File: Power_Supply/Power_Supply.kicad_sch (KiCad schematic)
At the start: 47 parts

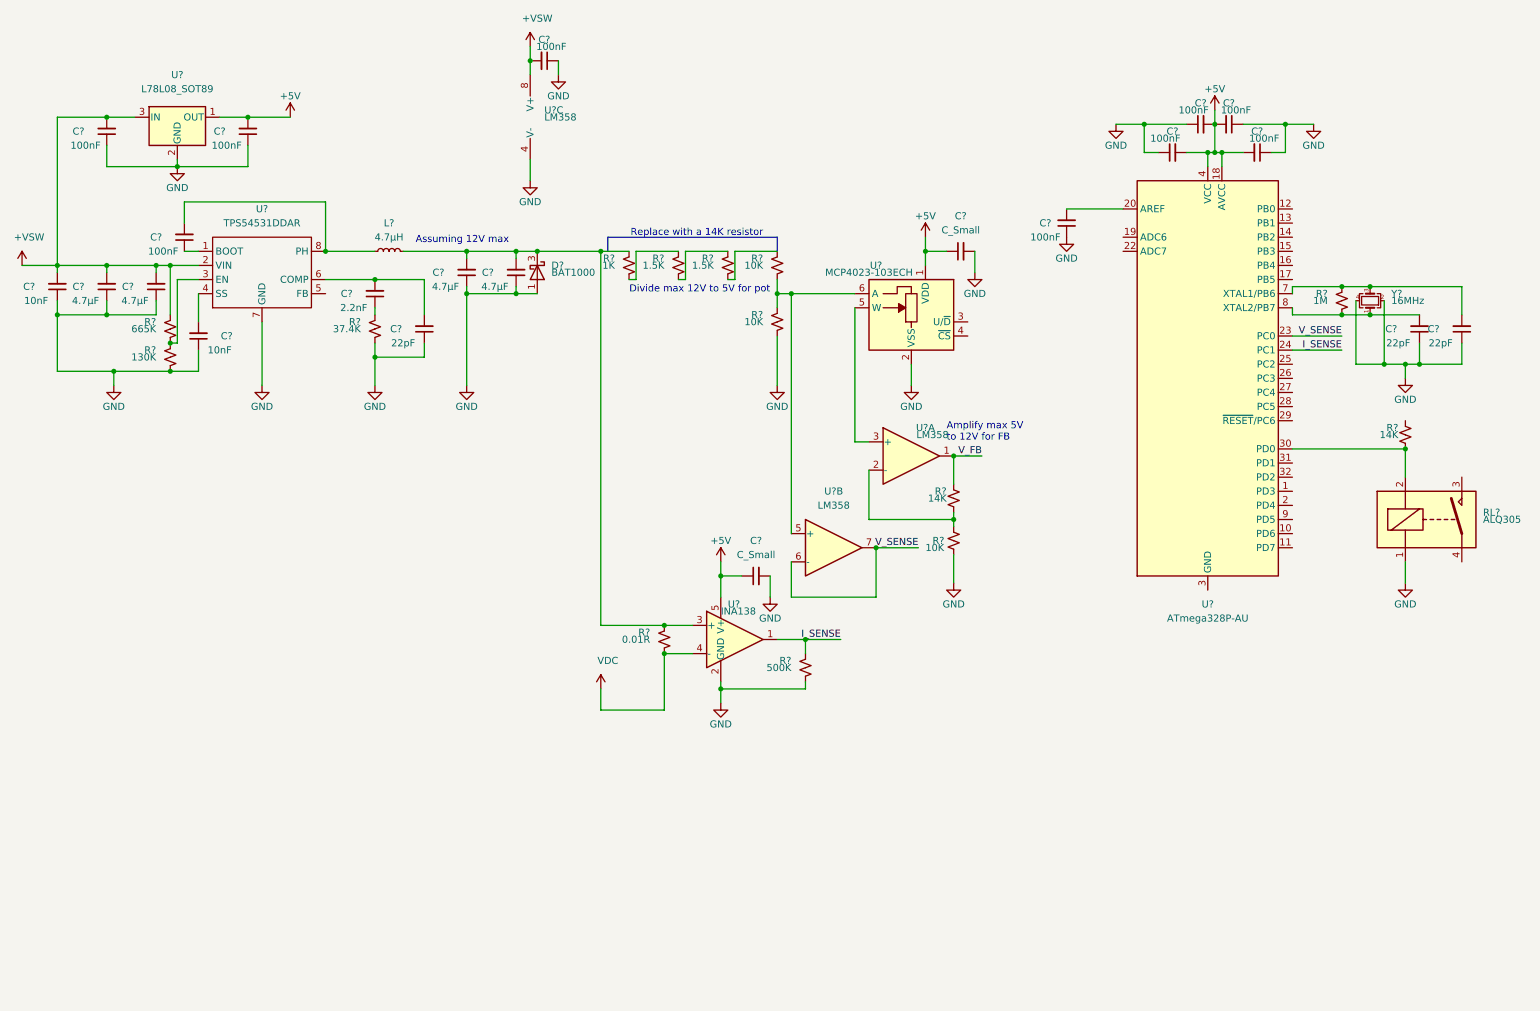
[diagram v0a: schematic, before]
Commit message: staring layout... need to add input connection
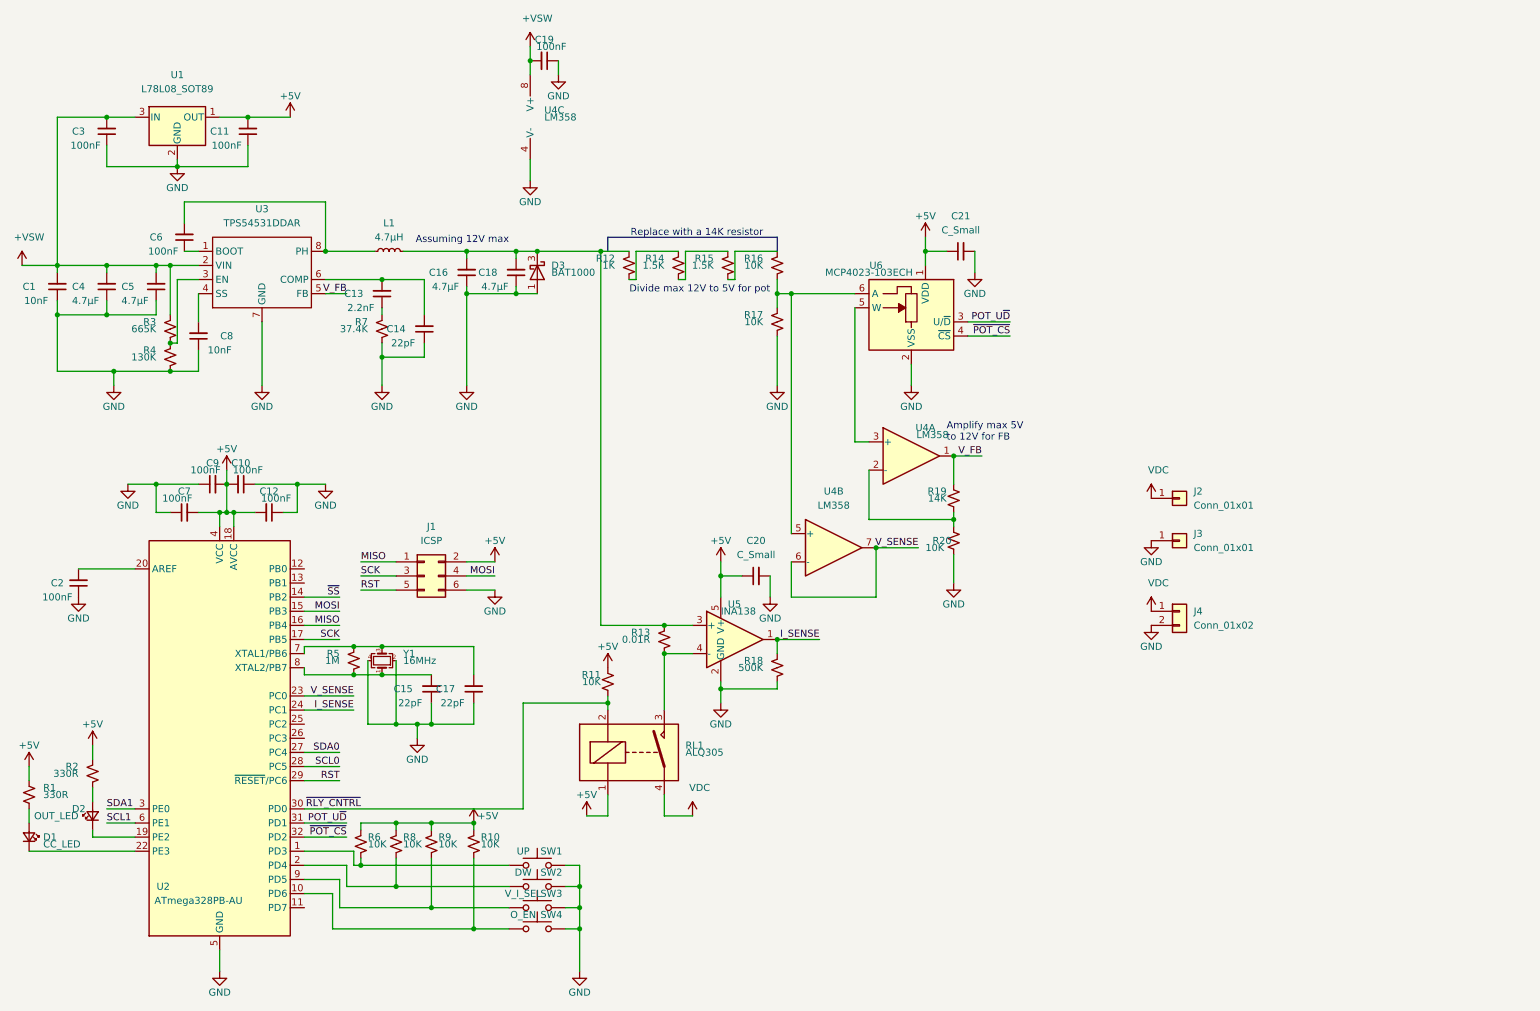
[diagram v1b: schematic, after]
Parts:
- added D1: CC_LED, LED_SMD:LED_0805_2012Metric, symbol Device:LED_Small
- added D2: OUT_LED, LED_SMD:LED_0805_2012Metric, symbol Device:LED_Small
- added J1: ICSP, Custom_Vertical_2x_2.54mm_Pin_Header:PinHeader_2x03_P2.54mm_Vertical, symbol Connector_Generic:Conn_02x03_Odd_Even
- added J2, J3: Conn_01x01, Binding_Post:Binding_Post, symbol Connector_Generic:Conn_01x01
- added J4: Conn_01x02, Custom_Vertical_1x_2.54mm_Pin_Header:PinHeader_1x02_P2.54mm_Vertical, symbol Connector_Generic:Conn_01x02
- added R1, R2: 330R, Resistor_SMD:R_0805_2012Metric, symbol Device:R_Small_US
- added R10, R6, R8, R9: 10K, Resistor_SMD:R_0805_2012Metric, symbol Device:R_Small_US
- added SW1: UP, Button_Switch_SMD:SW_SPST_TL3342, symbol Switch:SW_Push
- added SW2: DW, Button_Switch_SMD:SW_SPST_TL3342, symbol Switch:SW_Push
- added SW3: V_I_SEL, Button_Switch_SMD:SW_SPST_TL3342, symbol Switch:SW_Push
- added SW4: O_EN, Button_Switch_SMD:SW_SPST_TL3342, symbol Switch:SW_Push
- R11: renamed from R?; value 14K -> 10K
- U2: renamed from U?; value ATmega328P-AU -> ATmega328PB-AU; symbol MCU_Microchip_ATmega:ATmega328P-AU -> MCU_Microchip_ATmega:ATmega328PB-AU
- gave numbers to parts that had none: 43
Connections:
- net +5V: now also R11.1, RL1.1, J1.2 (Pin_2), R1.2, R10.1, R2.2, R6.1, R8.1, R9.1; no longer U2.6 (VCC)
- net GND: now also U2.21 (GND), U2.5 (GND), J1.6 (Pin_6), J3.1 (Pin_1), J4.2 (Pin_2), SW1.2, SW2.2, SW3.2, SW4.2; no longer RL1.1
- net VDC: now also RL1.4, J2.1 (Pin_1), J4.1 (Pin_1); no longer R13.1, U5.4 (-)
- net V_FB: now also U3.5 (FB)
- net ~RLY_CNTRL: now reaches R11.2, RL1.2, U2.30 (PD0)
- net at RL1.3: now also R13.1, U5.4 (-)
- net at U2.1 (PD3): now also R6.2, SW1.1
- net at U2.10 (PD6): now also R10.2, SW4.1
- net ~SS: now reaches U2.14 (PB2)
- net MOSI: now reaches U2.15 (PB3)
- net MOSI: now also J1.4 (Pin_4)
- net MISO: now reaches U2.16 (PB4)
- net MISO: now also J1.1 (Pin_1)
- net SCK: now reaches U2.17 (PB5)
- net SCK: now also J1.3 (Pin_3)
- net at U2.19 (PE2): now also D2.1 (K)
- net at U2.2 (PD4): now also R8.2, SW2.1
- net at U2.22 (PE3): now also D1.1 (K)
- net SDA0: now reaches U2.27 (PC4)
- net SCL0: now reaches U2.28 (PC5)
- net RST: now reaches U2.29 (~RESET~/PC6)
- net RST: now also J1.5 (Pin_5)
- net POT_U~D: now reaches U2.31 (PD1)
- net POT_U~D: now also U6.3 (U/~D)
- net ~POT_CS: now reaches U2.32 (PD2)
- net ~POT_CS: now also U6.4 (~CS)
- net at U2.9 (PD5): now also R9.2, SW3.1
- new net: D1.2 (A), R1.1
- new net: D2.2 (A), R2.1
- new net SCL1: U2.6 (PE1)
- new net SDA1: U2.3 (PE0)
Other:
- moved on the sheet: C10, C12, C13, C15, C17, C2, C7, C9, R11, R18, R5, R7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
